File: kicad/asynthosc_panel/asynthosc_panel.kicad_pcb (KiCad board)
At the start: 2 copper layers, 133.9 x 128.4 mm, 17 parts, among them J15 Conn_02x04_Odd_Even

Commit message: [PCB] Bit of cleanup
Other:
- board size 133.9 x 128.4 mm -> 72.1 x 128.4 mm
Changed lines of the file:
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@@
 			(at 0 3.15 0)
 			(layer "F.Fab")
+			(hide yes)
 			(effects
 				(font
@@
 			(layer "F.CrtYd")
 		)
-		(fp_text user "${REFERENCE}"
-			(at 0 0 0)
-			(layer "F.Fab")
-			(effects
-				(font
-					(size 1 1)
-					(thickness 0.15)
-				)
-			)
-		)
 		(pad "" np_thru_hole circle
 			(at 0 0)
@@
 			(at 0 3.15 0)
 			(layer "F.Fab")
+			(hide yes)
 			(effects
 				(font
@@
 			(layer "F.CrtYd")
 		)
-		(fp_text user "${REFERENCE}"
-			(at 0 0 0)
-			(layer "F.Fab")
-			(effects
-				(font
-					(size 1 1)
-					(thickness 0.15)
-				)
-			)
-		)
 		(pad "" np_thru_hole circle
 			(at 0 0)
@@
 			(at 0 3.15 0)
 			(layer "F.Fab")
+			(hide yes)
 			(effects
 				(font
@@
 			(layer "F.CrtYd")
 		)
-		(fp_text user "${REFERENCE}"
-			(at 0 0 0)
-			(layer "F.Fab")
-			(effects
-				(font
-					(size 1 1)
-					(thickness 0.15)
-				)
-			)
-		)
 		(pad "" np_thru_hole circle
 			(at 0 0)
@@
 			(at 0 3.15 0)
 			(layer "F.Fab")
+			(hide yes)
 			(effects
 				(font
@@
 			(layer "F.CrtYd")
 		)
-		(fp_text user "${REFERENCE}"
-			(at 0 0 0)
-			(layer "F.Fab")
-			(effects
-				(font
-					(size 1 1)
-					(thickness 0.15)
-				)
-			)
-		)
 		(pad "" np_thru_hole circle
 			(at 0 0)
@@
 	)
 	(gr_line
-		(start 37.24 65.92)
-		(end 37.24 60.92)
-		(stroke
-			(width 2)
-			(type default)
-		)
-		(layer "Edge.Cuts")
-	)
-	(gr_line
-		(start 37.24 65.92)
-		(end 40.49 65.92)
-		(stroke
-			(width 2)
-			(type default)
-		)
-		(layer "Edge.Cuts")
-	)
-	(gr_line
-		(start 37.49 69.92)
-		(end 40.49 69.92)
-		(stroke
-			(width 2)
-			(type default)
-		)
-		(layer "Edge.Cuts")
-	)
-	(gr_line
-		(start 37.49 71.42)
-		(end 37.49 69.92)
-		(stroke
-			(width 2)
-			(type default)
-		)
-		(layer "Edge.Cuts")
-	)
-	(gr_arc
-		(start 40.74 65.92)
-		(mid 42.74 67.92)
-		(end 40.74 69.92)
-		(stroke
-			(width 2)
-			(type default)
-		)
-		(layer "Edge.Cuts")
-	)
-	(gr_line
 		(start 99 65.8)
 		(end 99 60.8)
@@
 			(keep_text_aligned yes)
 		)
-		(gr_text "3.0000 mm"
+		(gr_text "3,0000 mm"
 			(at 114.4 51.505 90)
 			(layer "Eco1.User")
@@
 			(keep_text_aligned yes)
 		)
-		(gr_text "7.5000 mm"
+		(gr_text "7,5000 mm"
 			(at 103.75 45.650001 0)
 			(layer "Eco1.User")
@@
 			(keep_text_aligned yes)
 		)
-		(gr_text "71.1200 mm"
+		(gr_text "71,1200 mm"
 			(at 135.56 39.85 0)
 			(layer "Eco1.User")
@@
 			(keep_text_aligned yes)
 		)
-		(gr_text "128.4000 mm"
+		(gr_text "128,4000 mm"
 			(at 83.85 114.2 90)
 			(layer "Eco1.User")
@@
 			(keep_text_aligned yes)
 		)
-		(gr_text "R 2.0000 mm"
+		(gr_text "R 2,0000 mm"
 			(at 107.56 80.61 0)
 			(layer "User.1")
@@
 			(keep_text_aligned yes)
 		)
-		(gr_text "R 3.2000 mm"
+		(gr_text "R 3,2000 mm"
 			(at 124.56 89.85 0)
 			(layer "User.1")
@@
 			(keep_text_aligned yes)
 		)
-		(gr_text "R 4.4000 mm"
+		(gr_text "R 4,4000 mm"
 			(at 165.56 146.8 0)
 			(layer "User.1")
@@
 			(keep_text_aligned yes)
 		)
-		(gr_text "71.1200 mm"
+		(gr_text "71,1200 mm"
 			(at 135.56 34.85 0)
 			(layer "User.1")
@@
 			(keep_text_aligned yes)
 		)
-		(gr_text "17.5000 mm"
+		(gr_text "17,5000 mm"
 			(at 158.41 69.55 90)
 			(layer "User.1")
@@
 			(keep_text_aligned yes)
 		)
-		(gr_text "30.0000 mm"
+		(gr_text "30,0000 mm"
 			(at 115 166.85 0)
 			(layer "User.1")
@@
 			(keep_text_aligned yes)
 		)
-		(gr_text "46.2500 mm"
+		(gr_text "46,2500 mm"
 			(at 123.125 97.85 0)
 			(layer "User.1")
@@
 			(keep_text_aligned yes)
 		)
-		(gr_text "66.0000 mm"
+		(gr_text "66,0000 mm"
 			(at 133 192.85 0)
 			(layer "User.1")
@@
 			(keep_text_aligned yes)
 		)
-		(gr_text "108.8000 mm"
+		(gr_text "108,8000 mm"
 			(at 49.41 104.4 90)
 			(layer "User.1")
@@
 			(keep_text_aligned yes)
 		)
-		(gr_text "11.5000 mm"
+		(gr_text "11,5000 mm"
 			(at 160.41 89.8 90)
 			(layer "User.1")
@@
 			(keep_text_aligned yes)
 		)
-		(gr_text "63.6200 mm"
+		(gr_text "63,6200 mm"
 			(at 131.81 42.85 0)
 			(layer "User.1")
@@
 			(keep_text_aligned yes)
 		)
-		(gr_text "11.5000 mm"
+		(gr_text "11,5000 mm"
 			(at 152 80.85 0)
 			(layer "User.1")
@@
 			(keep_text_aligned yes)
 		)
-		(gr_text "52.0000 mm"
+		(gr_text "52,0000 mm"
 			(at 126 173.85 0)
 			(layer "User.1")
@@
 			(keep_text_aligned yes)
 		)
-		(gr_text "15.6000 mm"
+		(gr_text "15,6000 mm"
 			(at 93.41 170.6 90)
 			(layer "User.1")
@@
 			(keep_text_aligned yes)
 		)
-		(gr_text "3.0000 mm"
+		(gr_text "3,0000 mm"
 			(at 96.41 176.9 90)
 			(layer "User.1")
@@
 			(keep_text_aligned yes)
 		)
-		(gr_text "18.0000 mm"
+		(gr_text "18,0000 mm"
 			(at 109 61.85 0)
 			(layer "User.1")
@@
 			(keep_text_aligned yes)
 		)
-		(gr_text "128.4000 mm"
+		(gr_text "128,4000 mm"
 			(at 174.41 114.2 90)
 			(layer "User.1")
@@
 			(keep_text_aligned yes)
 		)
-		(gr_text "7.5000 mm"
+		(gr_text "7,5000 mm"
 			(at 106.56 45 0)
 			(layer "User.1")
@@
 			(keep_text_aligned yes)
 		)
-		(gr_text "46.7500 mm"
+		(gr_text "46,7500 mm"
 			(at 123.375 120.85 0)
 			(layer "User.1")
@@
 			(keep_text_aligned yes)
 		)
-		(gr_text "34.0500 mm"
+		(gr_text "34,0500 mm"
 			(at 80.41 67.025 90)
 			(layer "User.1")
@@
 			(keep_text_aligned yes)
 		)
-		(gr_text "3.0000 mm"
+		(gr_text "3,0000 mm"
 			(at 96.41 51.5 90)
 			(layer "User.1")
@@
 			(keep_text_aligned yes)
 		)
-		(gr_text "41.0000 mm"
+		(gr_text "41,0000 mm"
 			(at 120.5 169.85 0)
 			(layer "User.1")
@@
 			(keep_text_aligned yes)
 		)
-		(gr_text "35.0000 mm"
+		(gr_text "35,0000 mm"
 			(at 135.5 55.85 0)
 			(layer "User.1")
@@
 			(keep_text_aligned yes)
 		)
-		(gr_text "13.2500 mm"
+		(gr_text "13,2500 mm"
 			(at 106.625 88.85 0)
 			(layer "User.1")
@@
 			(keep_text_aligned yes)
 		)
-		(gr_text "13.7500 mm"
+		(gr_text "13,7500 mm"
 			(at 106.875 136.85 0)
 			(layer "User.1")
@@
 			(keep_text_aligned yes)
 		)
-		(gr_text "63.6200 mm"
+		(gr_text "63,6200 mm"
 			(at 131.81 187.85 0)
 			(layer "User.1")
@@
 			(keep_text_aligned yes)
 		)
-		(gr_text "5.4400 mm"
+		(gr_text "5,4400 mm"
 			(at 102.28 180.85 0)
 			(layer "User.1")
@@
 			(keep_text_aligned yes)
 		)
-		(gr_text "7.5000 mm"
+		(gr_text "7,5000 mm"
 			(at 103.75 184.85 0)
 			(layer "User.1")
@@
 			(keep_text_aligned yes)
 		)
-		(gr_text "19.0000 mm"
+		(gr_text "19,0000 mm"
 			(at 109.5 151.85 0)
 			(layer "User.1")
@@
 			(keep_text_aligned yes)
 		)
-		(gr_text "80.1000 mm"
+		(gr_text "80,1000 mm"
 			(at 66.41 90.05 90)
 			(layer "User.1")
@@
 			(keep_text_aligned yes)
 		)
-		(gr_text "39.8500 mm"
+		(gr_text "39,8500 mm"
 			(at 73.41 69.925 90)
 			(layer "User.1")
@@
 			(keep_text_aligned yes)
 		)
-		(gr_text "10.8000 mm"
+		(gr_text "10,8000 mm"
 			(at 115.41 55.4 90)
 			(layer "User.1")
@@
 			(keep_text_aligned yes)
 		)
-		(gr_text "35.5600 mm"
+		(gr_text "35,5600 mm"
 			(at 117.78 94.85 0)
 			(layer "User.1")
@@
 			(keep_text_aligned yes)
 		)
-		(gr_text "24.8000 mm"
+		(gr_text "24,8000 mm"
 			(at 91.41 62.4 90)
 			(layer "User.1")
@@
 			(keep_text_aligned yes)
 		)
-		(gr_text "96.8000 mm"
+		(gr_text "96,8000 mm"
 			(at 57.41 98.4 90)
 			(layer "User.1")

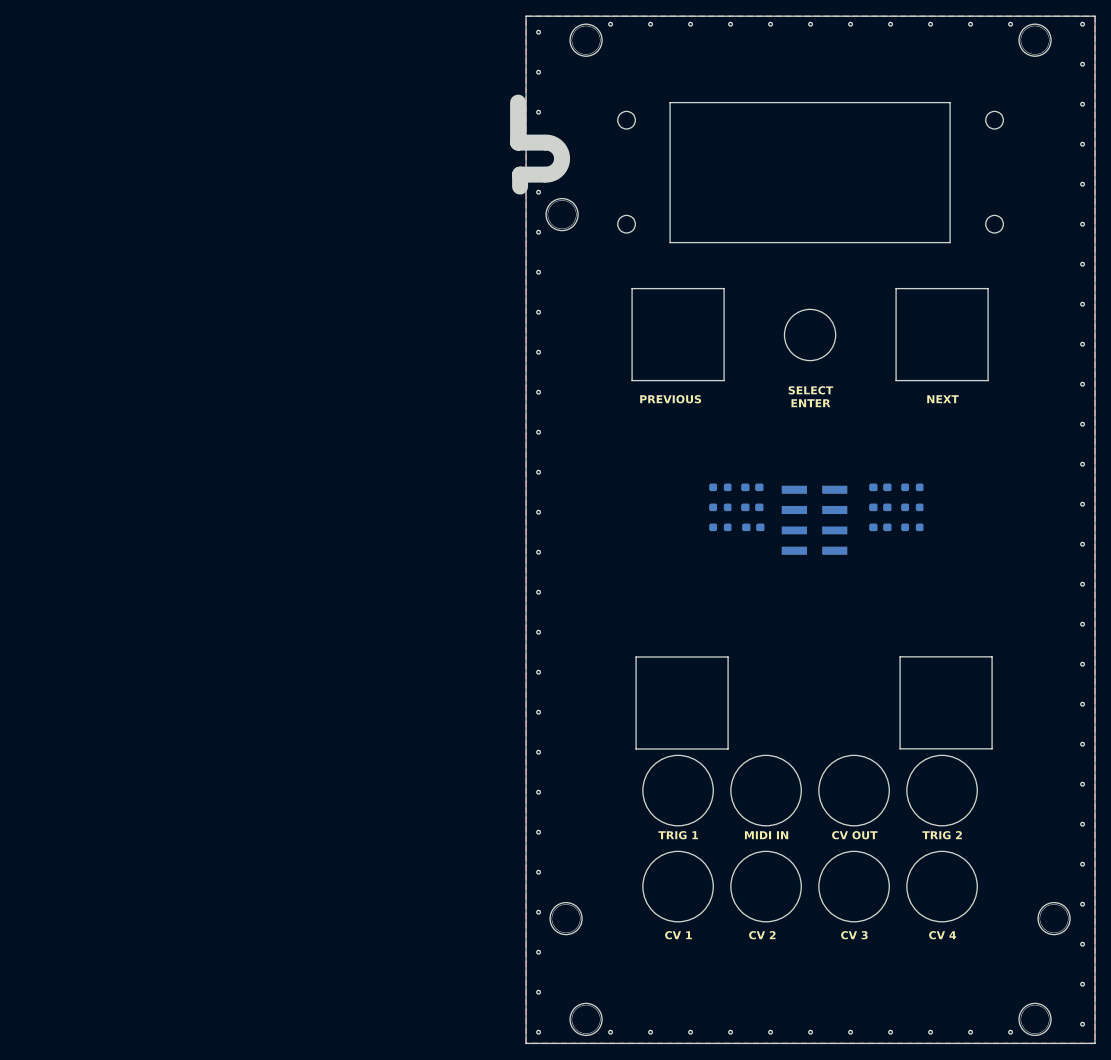
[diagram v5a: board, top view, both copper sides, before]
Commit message: [PCB] Integrate new design
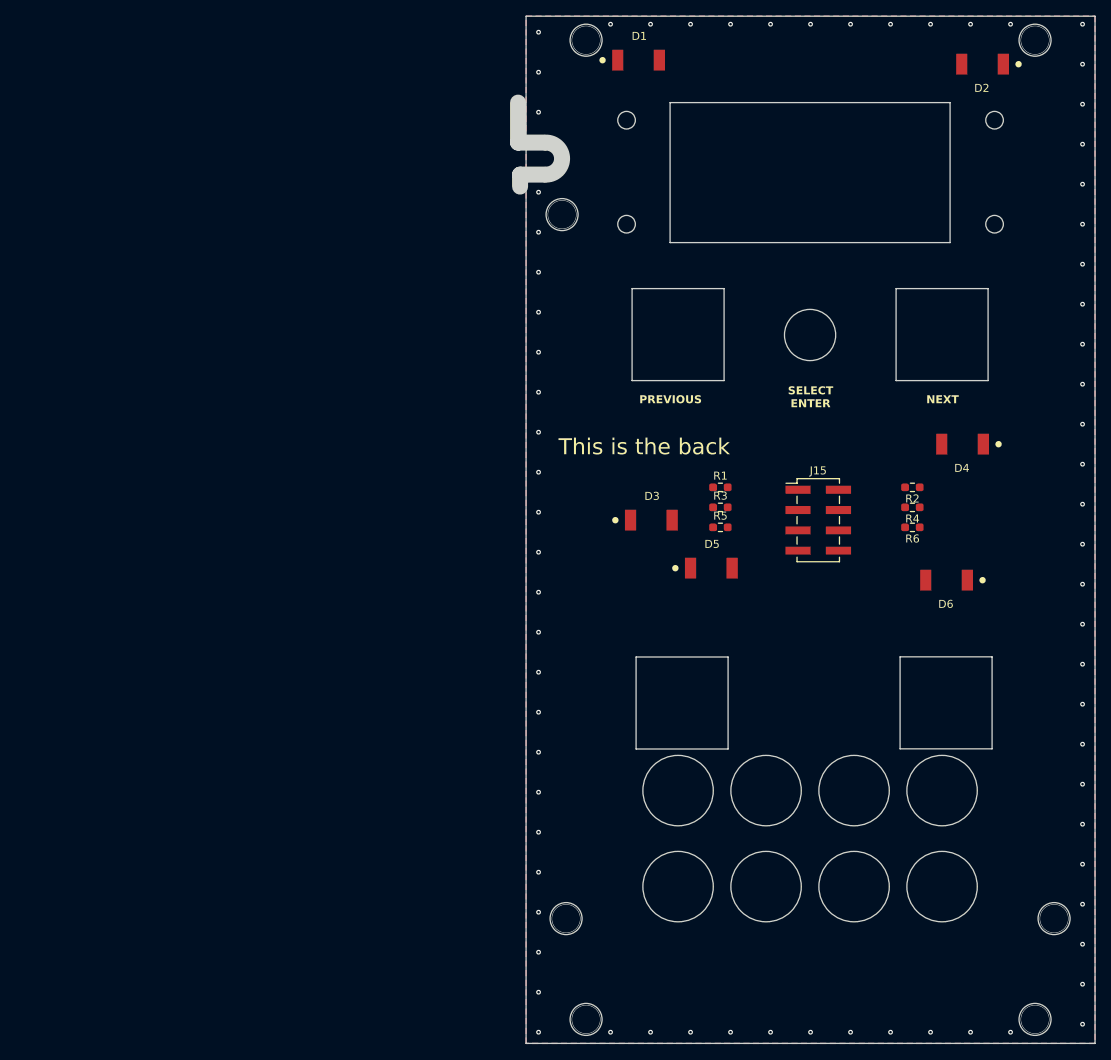
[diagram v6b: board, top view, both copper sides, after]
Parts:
- added REF**: LOGO_flower_A, asynthosc:LOGO_flower_A, B.Cu at (119.2, 51.0)
- added REF**: LOGO_flower_B, asynthosc:LOGO_flower_B, B.Cu at (161.8, 51.6)
- D1, D2, D3, D4, D5, D6: value LED Red 0603 -> Reverse LED; footprint LED_SMD:LED_0603_1608Metric_Pad1.05x0.95mm_HandSolder -> asynthosc:LED_Sunled_XZxx45x-9_nohole; moved to F.Cu
- J15, R1, R2, R3, R4, R5, R6: moved to F.Cu
- moved D1 61.4 mm to (114.1, 55.5), turned to 0 degrees
- moved D2 60.2 mm to (157.1, 56.0), turned to 180 degrees
- moved D3 28.7 mm to (115.7, 113.0), turned to 0 degrees
- moved D4 27.4 mm to (154.6, 103.5), turned to 180 degrees
- moved D6 25.0 mm to (152.6, 120.5), turned to 180 degrees
- moved R1 24.0 mm to (124.3, 108.9), turned to 0 degrees
- moved R2 24.0 mm to (148.3, 108.9), turned to 180 degrees
- moved R3 24.0 mm to (124.3, 111.4), turned to 0 degrees
- moved R4 24.0 mm to (148.3, 111.4), turned to 180 degrees
- moved R5 24.0 mm to (124.3, 113.9), turned to 0 degrees
- moved R6 24.0 mm to (148.3, 113.9), turned to 180 degrees
- moved D5 21.7 mm to (123.2, 119.0), turned to 0 degrees
- moved J15 0.46 mm to (136.5, 113.0), turned to 0 degrees
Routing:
- net Net-(D4-K): vias 0 -> 1
- net (no net): vias 7 -> 6
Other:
- board text added: "1"
- board text added: "2"
- board text added: "3"
- board text added: "4"
- board text added: "MIDI"
- board text added: "T1"
- board text added: "T2"
- board text added: "This is the back"
- board text added: "aSynth2OSC"
- board text removed: "CV 1"
- board text removed: "CV 2"
- board text removed: "CV 3"
- board text removed: "CV 4"
- board text removed: "CV OUT"
- board text removed: "MIDI IN"
- board text removed: "TRIG 1"
- board text removed: "TRIG 2"
- board text removed: "This actually is front"

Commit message: [PANEL] Decorative stuff
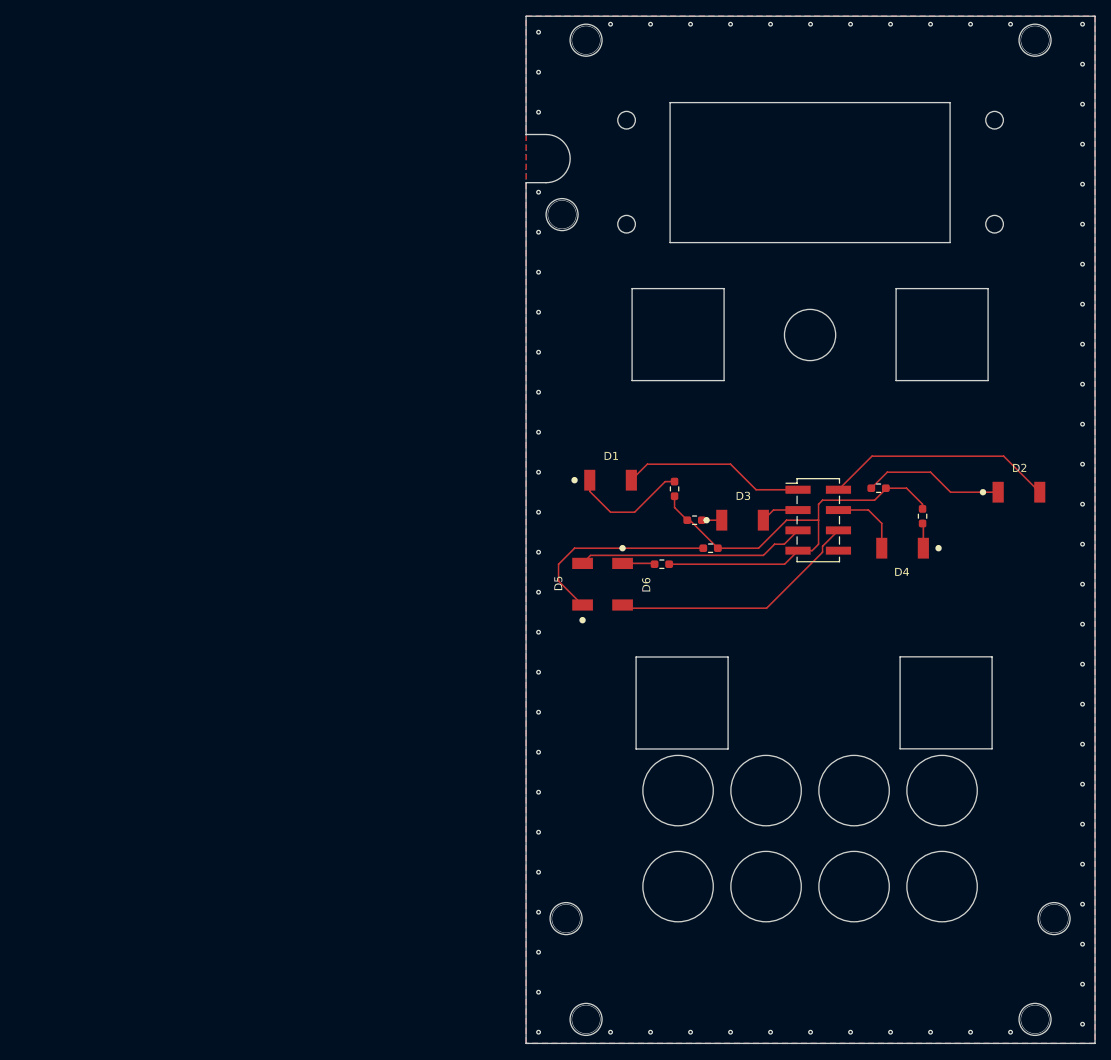
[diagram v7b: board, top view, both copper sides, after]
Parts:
- added REF**: LOGO_flower_A, asynthosc:LOGO_flower_A, B.Cu at (151.7, 112.0)
- added REF**: LOGO_cat, asynthosc:LOGO_cat, B.Cu at (122.6, 51.0)
- added REF**: LOGO_cat_rotated, asynthosc:LOGO_cat_rotated, B.Cu at (156.3, 51.0)
- added REF**: Val**, asynthosc:LOGO_asynthosc_transparent, B.Cu at (109.6, 123.5)
- added REF**: LOGO_flower_B, asynthosc:LOGO_flower_B, B.Cu at (131.8, 108.6)
- moved REF** 53.7 mm to (166.4, 105.1)
- moved D2 53.7 mm to (161.6, 109.5), turned to 0 degrees
- moved REF** 52.6 mm to (115.7, 103.5)
- moved D1 52.6 mm to (110.6, 108.0)
- moved D6 40.5 mm to (112.1, 121.0), turned to -90 degrees
- moved R6 31.7 mm to (117.0, 118.5)
- moved D5 16.2 mm to (107.1, 121.0), turned to 90 degrees
- moved D4 15.0 mm to (147.1, 116.5)
- moved D3 11.4 mm to (127.1, 113.0)
- moved R1 5.74 mm to (118.6, 109.1), turned to 90 degrees
- moved R2 4.23 mm to (144.1, 109.0)
- moved R3 3.61 mm to (121.1, 113.0)
- moved R5 2.88 mm to (123.1, 116.5), turned to 180 degrees
- moved R4 1.68 mm to (149.6, 112.5), turned to -90 degrees
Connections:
- J15 pad 7: 3V3 -> +3V3
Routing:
- net +3V3: track 0.00 -> 63.0 mm
- net /EXT_LED6: track 0.00 -> 31.6 mm
- net /EXT_LED2: track 0.00 -> 28.8 mm
- net /EXT_LED5: track 0.00 -> 28.7 mm
- net Net-(D5-K): track 0.00 -> 25.2 mm
- net /EXT_LED1: track 0.00 -> 23.0 mm
- net Net-(D2-K): track 0.00 -> 17.8 mm
- net Net-(D1-K): track 0.00 -> 14.7 mm
- net /EXT_LED4: track 0.00 -> 9.20 mm
- net /EXT_LED3: track 0.00 -> 4.87 mm
- net Net-(D6-K): track 0.00 -> 4.04 mm
- net Net-(D4-K): track 0.00 -> 3.13 mm, vias 1 -> 0
- net Net-(D3-K): track 0.00 -> 2.49 mm
- net (no net): vias 6 -> 7
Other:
- board size 72.1 x 128.4 mm -> 71.1 x 128.4 mm
- board text removed: "NEXT"
- board text removed: "PREVIOUS"
- board text removed: "SELECT ENTER"
- board text removed: "This is the back"
